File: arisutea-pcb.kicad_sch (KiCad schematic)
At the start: 46 parts, among them J1 PROG, Q1 2N7002, U1 STM32F072-LQFP48, U2 NUF2221W1T2G, U3 TLV70233

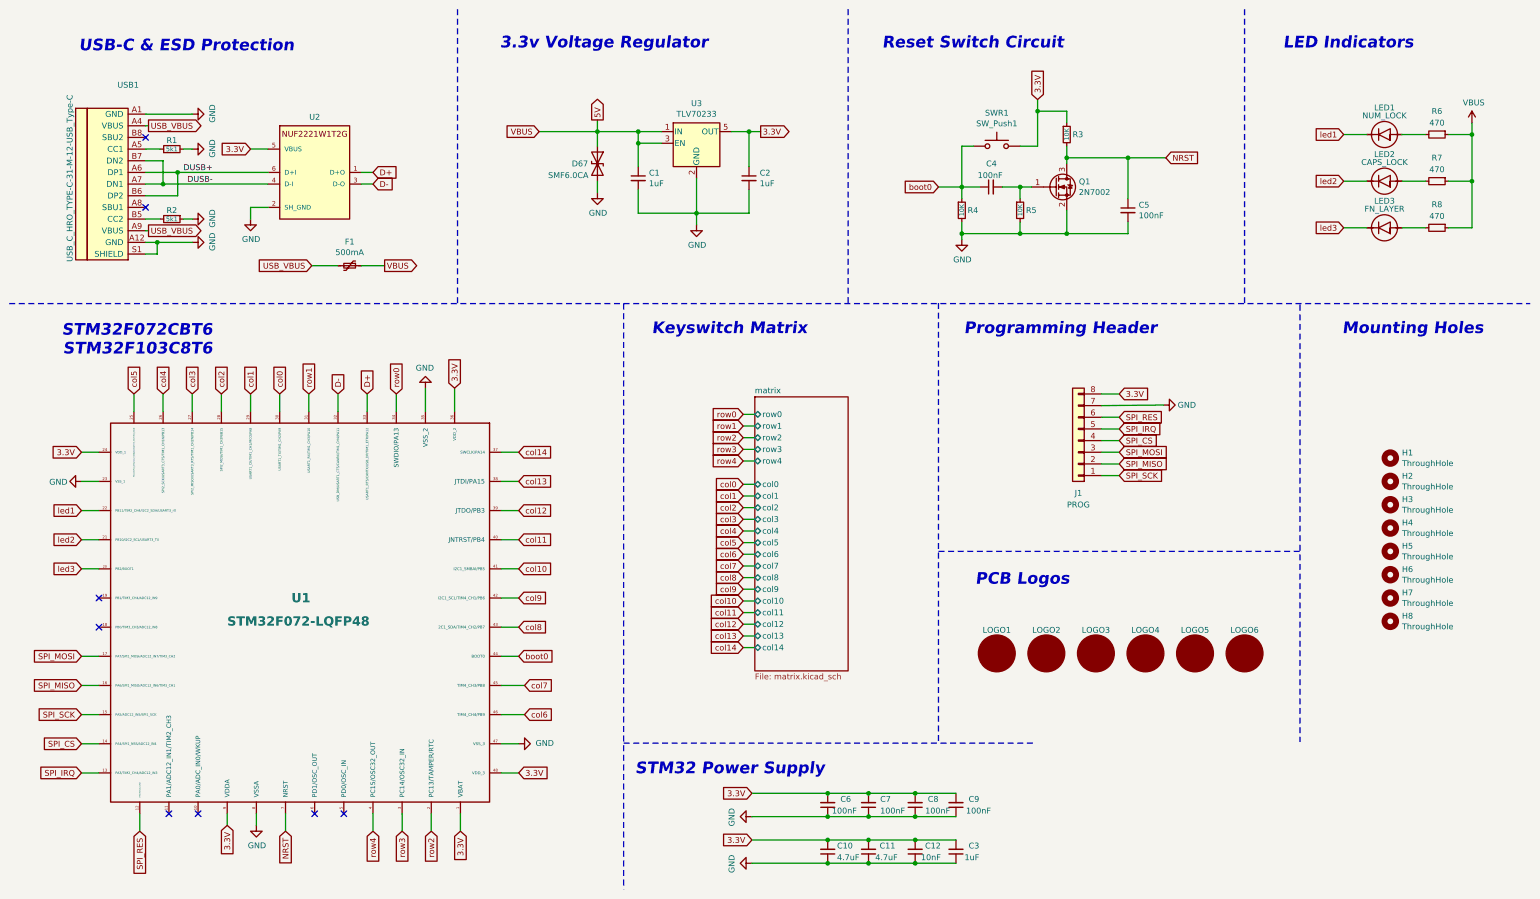
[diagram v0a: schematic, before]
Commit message: rev0.4 update
Small update to fix some non critical things.
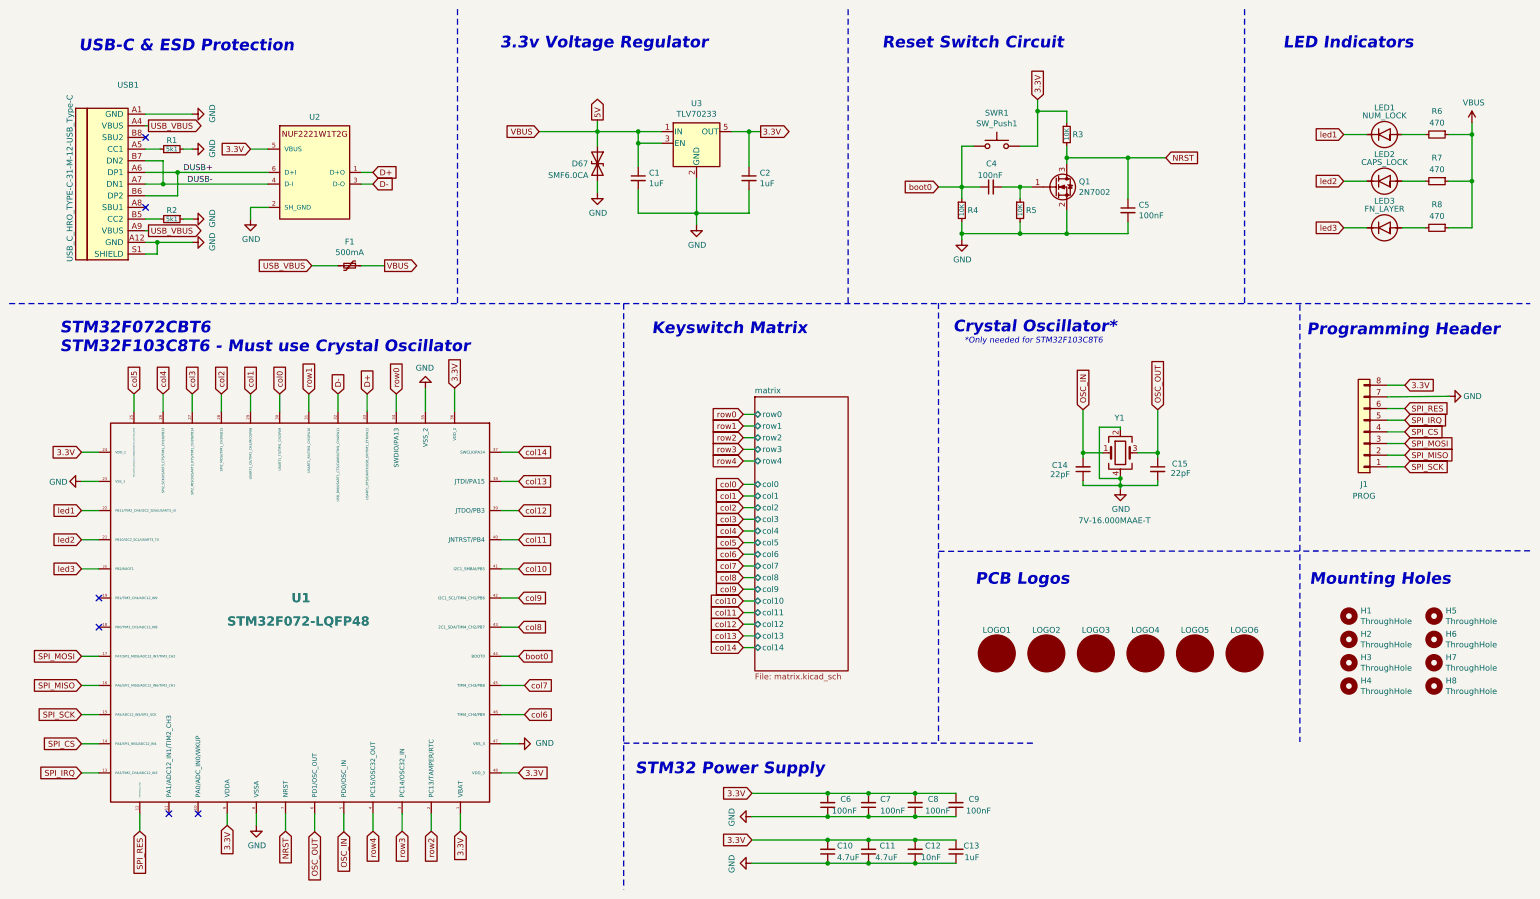
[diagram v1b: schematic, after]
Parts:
- added C14, C15: 22pF, arisutea-STM32:C_0805_2012Metric_Pad1.18x1.45mm_HandSolder, symbol Device:C_Small
- added Y1: 7V-16.000MAAE-T, arisutea-STM32:Crystal_SMD_TXC_7M-4Pin_3.2x2.5mm_HandSoldering, symbol arisutea-stm32:Device_Crystal_GND24
- renumbered C3 to C13
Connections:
- net GND: now also C14.1, C15.2, Y1.2, Y1.4
- net OSC_IN: now reaches U1.5 (PD0/OSC_IN)
- net OSC_IN: now also C14.2, Y1.1
- net OSC_OUT: now reaches U1.6 (PD1/OSC_OUT)
- net OSC_OUT: now also C15.1, Y1.3
- no-connect marks 8 -> 6
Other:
- note added: "*Only needed for STM32F103C8T6"
- note added: "Crystal Oscillator*"
- note added: "STM32F072CBT6 STM32F103C8T6 - Must use Crystal Oscillator"
- note removed: "STM32F072CBT6 STM32F103C8T6"
- moved on the sheet: H1, H2, H3, H4, H5, H6, H7, H8, J1

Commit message: Add logo, edit ibom and readme
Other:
- company: 3x6 Design -> mattyams
